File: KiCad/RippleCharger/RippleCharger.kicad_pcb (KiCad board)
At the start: 2 copper layers, 190.2 x 195.3 mm, 123 parts, among them J1 Screw_Terminal_01x02, J2 AD9833, J3 UART1, J4 UART2, J5 bat+, J6 bat-, J7 Load, Q1 2N3904, Q2 2N3904, Q3 TIP41C, Q4 2N3904, Q5 2N3904, Q6 2N3904, SW1 SW_SPDT, U1 L7805, U2 LM358, U3 LM358, U4 LM358, U5 LM358, U6 LM358, U7 LAUNCHXL-F280049C, U8 INA282, U9 LM317_TO-263

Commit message: Update PCB layout m include relay footprint, board outlook.Modify Main 0049 code and add CV function
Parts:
- removed HS1: Heatsink, Heatsink:Heatsink_Fischer_SK104-STCB_35x13mm__2xDrill3.5mm_ScrewM3
- removed J1: Screw_Terminal_01x02, TerminalBlock:TerminalBlock_Altech_AK300-2_P5.00mm
- removed J7: Load, TerminalBlock:TerminalBlock_Altech_AK300-2_P5.00mm
- removed R39, R40: 10, Resistor_THT:R_Axial_Power_L20.0mm_W6.4mm_P25.40mm
- removed REF** (x4): MountingHole_2.5mm_Pad, MountingHole:MountingHole_2.5mm_Pad
- removed RGND: 0, Resistor_SMD:R_0805_2012Metric_Pad1.20x1.40mm_HandSolder
- removed SW1: SW_SPDT, basic:MTS-102
- added C14: 0.1u, Capacitor_SMD:C_0805_2012Metric_Pad1.18x1.45mm_HandSolder, B.Cu at (203.0, 96.8)
- added C15: 0.1u, Capacitor_SMD:C_0805_2012Metric_Pad1.18x1.45mm_HandSolder, B.Cu at (149.9, 99.1)
- added C16: 0.1u, Capacitor_SMD:C_0805_2012Metric_Pad1.18x1.45mm_HandSolder, B.Cu at (213.4, 99.1)
- added H1: MountingHole, MountingHole:MountingHole_3.2mm_M3_DIN965_Pad_TopBottom, F.Cu at (6.71, 5.13)
- added H2: MountingHole, MountingHole:MountingHole_3.2mm_M3_DIN965_Pad_TopBottom, F.Cu at (6.71, 143.6)
- added H3: MountingHole, MountingHole:MountingHole_3.2mm_M3_DIN965_Pad_TopBottom, F.Cu at (280.4, 5.38)
- added H4: MountingHole, MountingHole:MountingHole_3.2mm_M3_DIN965_Pad_TopBottom, F.Cu at (280.4, 143.8)
- added P1: IOPad, basic:IOPad, F.Cu at (20.4, 39.7)
- added P2: IOPad, basic:IOPad, F.Cu at (20.4, 59.2)
- added P3: Load+, basic:IOPad, F.Cu at (70.3, 118.3)
- added P4: Load-, basic:IOPad, F.Cu at (86.6, 118.2)
- added R44: 1k, Resistor_SMD:R_0805_2012Metric_Pad1.20x1.40mm_HandSolder, B.Cu at (198.9, 94.5)
- added R45: 1k, Resistor_SMD:R_0805_2012Metric_Pad1.20x1.40mm_HandSolder, B.Cu at (145.8, 96.8)
- added R46: 1k, Resistor_SMD:R_0805_2012Metric_Pad1.20x1.40mm_HandSolder, B.Cu at (209.3, 96.8)
- added R47: 10k, Resistor_SMD:R_0805_2012Metric_Pad1.20x1.40mm_HandSolder, B.Cu at (205.3, 99.1)
- added R48: 20k, Resistor_SMD:R_0805_2012Metric_Pad1.20x1.40mm_HandSolder, B.Cu at (209.3, 99.1)
- added TP4: Iprob-, Connector_PinHeader_2.54mm:PinHeader_1x01_P2.54mm_Vertical, F.Cu at (138.9, 83.8)
- added TP4: Iprob-, Connector_PinHeader_2.54mm:PinHeader_1x01_P2.54mm_Vertical, F.Cu at (61.4, 9.17)
- C10, C11, C13, C2, C3, C4, C5, C6, C7, C8, FB1, R10, R11, R12, R13, R14, R15, R16, R17, R18, R19, R2, R20, R21, R22, R24, R27, R3, R4, R5, R6, R7, R8, R9, U1, U2, U3, U4, U5, U6, U9: moved to F.Cu
- D10, D11, D12, D15, D17, D18, D5, D7, D8, D9: footprint Diode_SMD:D_0805_2012Metric_Pad1.15x1.40mm_HandSolder -> Diode_SMD:D_SOD-123
- D2, D3, D4: footprint Diode_SMD:D_0805_2012Metric_Pad1.15x1.40mm_HandSolder -> Diode_SMD:D_SOD-123; moved to F.Cu
- Q1, Q2, Q4, Q5, Q6: value 2N3904 -> MMBT3904
- R23, R26, R38: value 5.6k -> 1k
- R25: value 240 -> 200; moved to F.Cu
- R28, R33, R34: moved to B.Cu
- R36: value 100m -> 50m
- R42: value 5.6k -> 1k; moved to F.Cu
- TP1: value ac_wave -> Asymm
- TP2: value asymm -> base
- TP3: value CV -> Iprob+
- moved C10 176.8 mm to (31.8, 55.0), turned to 270 degrees
- moved R33 176.1 mm to (53.3, 15.0), turned to 180 degrees
- moved Q4 175.7 mm to (53.3, 17.9)
- moved D15 174.9 mm to (57.1, 17.9)
- moved J4 171.1 mm to (214.7, 84.1), turned to 90 degrees
- moved RY2 170.5 mm to (55.8, 26.1)
- moved D13 170.3 mm to (54.3, 18.1), turned to 270 degrees
- moved R38 169.8 mm to (53.3, 21.4), turned to 180 degrees
- moved J3 163.2 mm to (151.2, 83.8), turned to 90 degrees
- moved Cs1 158.0 mm to (21.3, 81.0), turned to 180 degrees
- moved U7 157.9 mm to (224.8, 94.3), turned to 180 degrees
- moved J2 154.1 mm to (27.9, 94.4), turned to 90 degrees
- moved R3 153.4 mm to (25.8, 88.0), turned to 0 degrees
- moved R41 150.8 mm to (81.4, 109.5)
- moved D16 150.3 mm to (78.1, 109.5)
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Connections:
- D10 pad 1: Vbat+ -> Net-(D10-Pad1)
- D11 pad 2: Iout -> Net-(D11-Pad2)
- D12 pad 1: Iout -> Net-(D11-Pad2)
- D16 pad 2: Net-(D16-Pad2) -> disChar
- D7 pad 2: Vbat- -> Net-(D7-Pad2)
- D8 pad 1: Vbat- -> Net-(D7-Pad2)
- D9 pad 2: Vbat+ -> Net-(D10-Pad1)
- Q1 pad 1: GND -> Net-(Q1-Pad1)
- Q1 pad 2: Net-(Q1-Pad2) -> GND
- Q3 pad 1: Net-(Q2-Pad1) -> Net-(Q2-Pad2)
- Q4 pad 1: GND -> Net-(Q4-Pad1)
- Q4 pad 2: Net-(Q4-Pad2) -> GND
- Q5 pad 1: GND -> Net-(Q5-Pad1)
- Q5 pad 2: Net-(Q5-Pad2) -> GND
- Q6 pad 1: GND -> Net-(Q6-Pad1)
- Q6 pad 2: Net-(Q6-Pad2) -> GND
- R23 pad 2: Net-(Q1-Pad2) -> Net-(Q1-Pad1)
- R26 pad 2: Net-(Q6-Pad2) -> Net-(Q6-Pad1)
- R29 pad 2: Vbat- -> Net-(D7-Pad2)
- R30 pad 1: Vbat- -> Net-(D7-Pad2)
- R31 pad 2: Vbat+ -> Net-(D10-Pad1)
- R32 pad 1: Vbat+ -> Net-(D10-Pad1)
- R35 pad 1: Net-(Q2-Pad2) -> Net-(Q2-Pad1)
- R36 pad 1: Net-(R36-Pad1) -> Iprob
- R38 pad 2: Net-(Q4-Pad2) -> Net-(Q4-Pad1)
- R42 pad 2: Net-(Q5-Pad2) -> Net-(Q5-Pad1)
- RV6 pad 1: Net-(RV6-Pad1) -> base
- RY1 pad 16: Net-(D5-Pad2) -> Net-(D15-Pad2)
- RY1 pad 4: sigout -> bat+
- RY1 pad 6: sigRly -> mid
- RY1 pad 8: asymm -> EIS
- RY2 pad 16: Net-(D15-Pad2) -> Net-(D17-Pad2)
- RY2 pad 4: mid -> Iprob
- RY2 pad 6: bat+ -> disChar
- RY2 pad 8: EIS -> Charge
- RY3 pad 16: Net-(D17-Pad2) -> Net-(D5-Pad2)
- RY3 pad 4: disChar -> sigRly
- RY3 pad 6: Net-(R36-Pad1) -> sigout
- RY3 pad 8: Charge -> asymm
- RY4 pad 4: +9V -> Charge
- RY4 pad 6: Charge -> +9V
- TP1 pad 1: Net-(Cs1-Pad1) -> asymm
- TP2 pad 1: asymm -> base
- TP3 pad 1: CV -> Iprob
- U7 pad 26: Iout -> Viout
- U7 pad 34: Rly1 -> Net-(U7-Pad34)
- U7 pad 35: Net-(U7-Pad35) -> Rly1
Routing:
- net disChar: track 0.00 -> 135.3 mm, vias 0 -> 1
- net +9V: track 0.00 -> 128.3 mm, vias 0 -> 2
- net Rly3: track 86.5 -> 200.6 mm, vias 2 -> 3
- net Vbat-: track 112.9 -> 6.72 mm, vias 2 -> 0
- net (no net): track 9.78 -> 111.6 mm
- net +3V3: track 12.9 -> 111.4 mm
- net EIS: track 0.00 -> 92.9 mm
- net sigout: track 58.4 -> 146.1 mm, vias 1 -> 4
- net GND: track 144.5 -> 226.6 mm, vias 11 -> 15
- net bat+: track 270.9 -> 189.0 mm, vias 2 -> 0
- net CV: track 145.2 -> 64.7 mm, vias 0 -> 1
- net MOSI1: track 130.2 -> 210.7 mm
- net Iout: track 263.0 -> 182.6 mm, vias 5 -> 2
- net CS1: track 149.5 -> 228.9 mm
- net Rly1: track 167.6 -> 230.1 mm
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- removed copper zone on B.Cu, net +5VD
- removed copper zone on B.Cu, net +9V
- removed copper zone on B.Cu, net CV
- removed copper zone on B.Cu, net EIS
- removed copper zone on B.Cu, net bat-
- removed copper zone on B.Cu, net disChar
- removed copper zone on B.Cu, net sigout
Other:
- board size 190.2 x 195.3 mm -> 295 x 150 mm
- rule trace_min: 0.1778 -> 0.2
- board text added: "/340"
- board text added: "4.2V"
- board text added: "Amp+"
- board text added: "Amp-"
- board text added: "CC cur"
- board text added: "Discharging"
- board text added: "INA282 OUT"
- board text added: "Ibat <-"
- board text added: "LED R1 R2 R3 R4"
- board text added: "Load+"
- board text added: "Load-"
- board text added: "OFF R2 Dischg CC Symm"
- board text added: "ON EIS Charg CV Asym"
- board text added: "SCIA 5V TX RX GND"
- board text added: "SCIB 5V TX RX GND"
- board text added: "Sigout"
- board text added: "Sinusoidal Ripple Charging Board Version: v1.6 Fix some footprint, Add current probe test point Author: CHUN-LIN CHEN Date: 2021/10/12"
- board text added: "TotAmp"
- board text added: "USB"
- board text added: "VR setup"
- board text added: "asy"
- board text added: "bat+"
- board text added: "bat-"
- board text added: "bias"
- board text added: "sin/cc"
- board text removed: "+5V"
- board text removed: "4.2V Voltage Source"
- board text removed: "ACSIG"
- board text removed: "Asymm"
- board text removed: "BAT+"
- board text removed: "BAT-"
- board text removed: "CC ADJ"
- board text removed: "CC/CV CHARGING"
- board text removed: "CHARGE/DISCHARGE"
- board text removed: "COM1"
- board text removed: "COM2"
- board text removed: "CV"
- board text removed: "DC BIAS"
- board text removed: "EIS"
- board text removed: "EIS MEASURE"
- board text removed: "HOT WHEN DISCHARGING"
- board text removed: "IOUT"
- board text removed: "LIMIT RESISTOR"
- board text removed: "MODE"
- board text removed: "NEG AMP"
- board text removed: "POS AMP"
- board text removed: "RX"
- board text removed: "SCIA"
- board text removed: "SCIB"
- board text removed: "SIN/CC MODE"
- board text removed: "SUMAPM"
- board text removed: "Sinusoidal Ripple Charging Board Version: v1.5 Discription: Add asymmectrical sinewave generator, INA282 current sensor, EIS measureing using UART interface. Author: CHUN-LIN CHEN Date: 2021/09/14"
- board text removed: "Symm/Asymm"
- board text removed: "TX"

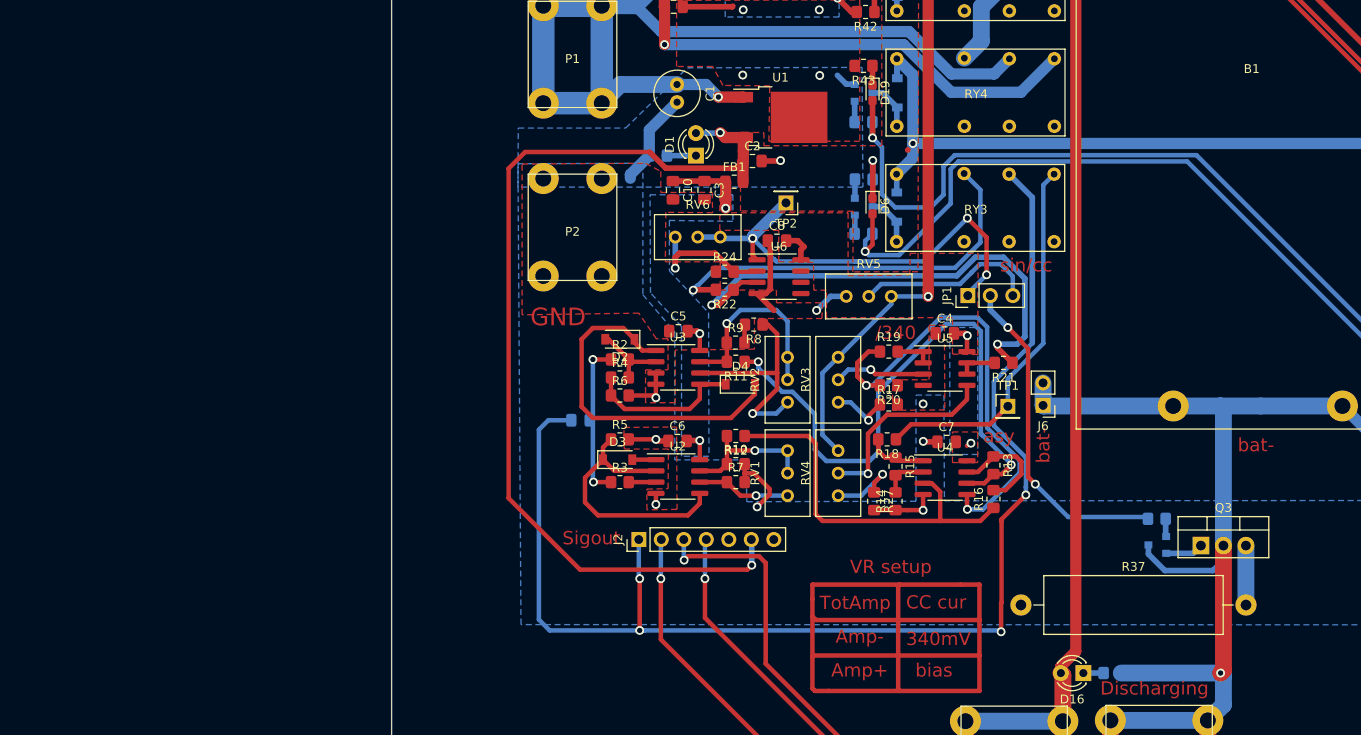
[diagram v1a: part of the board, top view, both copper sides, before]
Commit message: Fix CV charging route
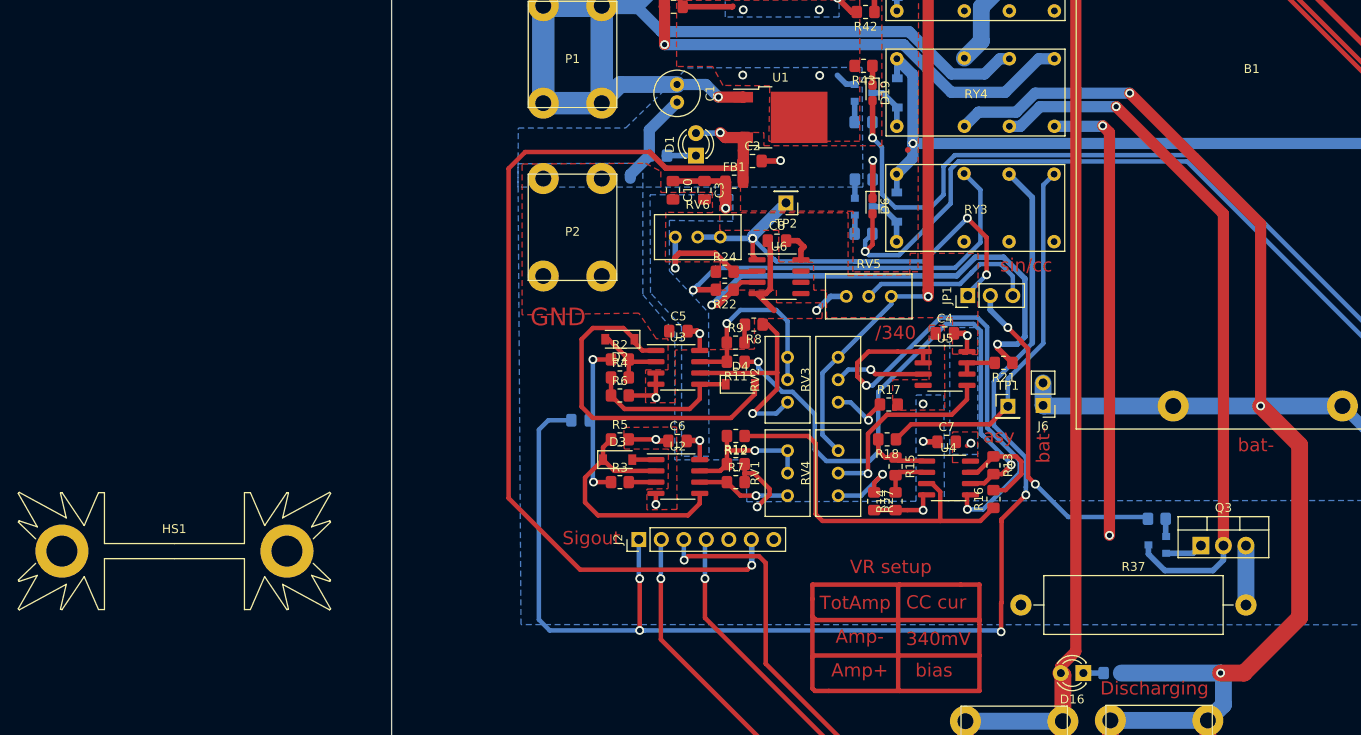
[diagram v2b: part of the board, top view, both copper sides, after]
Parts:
- removed R19, R20: 1k, Resistor_SMD:R_0805_2012Metric_Pad1.20x1.40mm_HandSolder
- added HS1: Heatsink, Heatsink:Heatsink_Fischer_SK104-STCB_35x13mm__2xDrill3.5mm_ScrewM3, F.Cu at (-24.5, 95.8)
- RV1, RV3: value 20k -> 50k
- moved U4 0.40 mm to (62.9, 87.5)
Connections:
- Q2 pad 3: bat- -> bat-2
- Q3 pad 2: bat- -> bat-2
- RY4 pad 11: Net-(RY4-Pad11) -> bat-2
- RY4 pad 13: Net-(RY4-Pad13) -> bat-
- RY4 pad 9: Net-(RY4-Pad9) -> GND
- U5 pad 1: Net-(R19-Pad2) -> 340mV
- U5 pad 2: Net-(R19-Pad2) -> 340mV
- U7 pad 32: Rly3 -> Net-(U7-Pad32)
- U7 pad 34: Net-(U7-Pad34) -> Rly3
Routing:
- net bat-2: track 0.00 -> 79.9 mm, vias 0 -> 1
- net bat-: track 247.3 -> 303.4 mm, vias 1 -> 3
- net GND: track 226.6 -> 278.7 mm, vias 15 -> 17
- net 340mV: track 52.1 -> 56.7 mm
- net Net-(R19-Pad2): track 4.15 -> 0.00 mm
